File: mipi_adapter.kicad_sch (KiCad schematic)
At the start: 0 parts

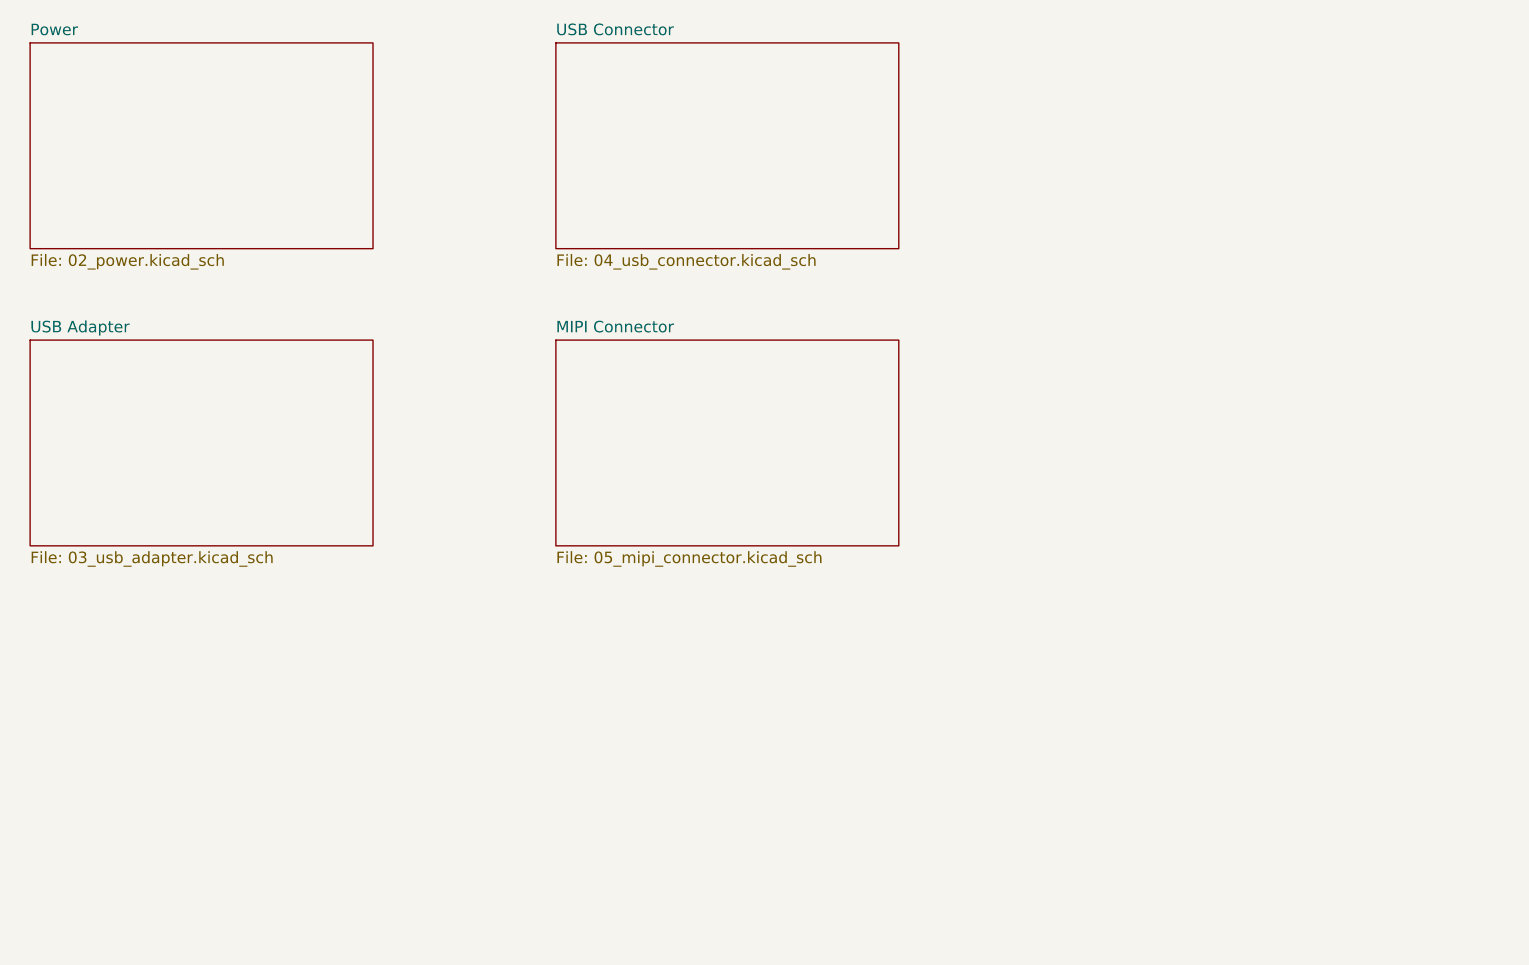
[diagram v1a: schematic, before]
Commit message: finished usb interface and added some new components
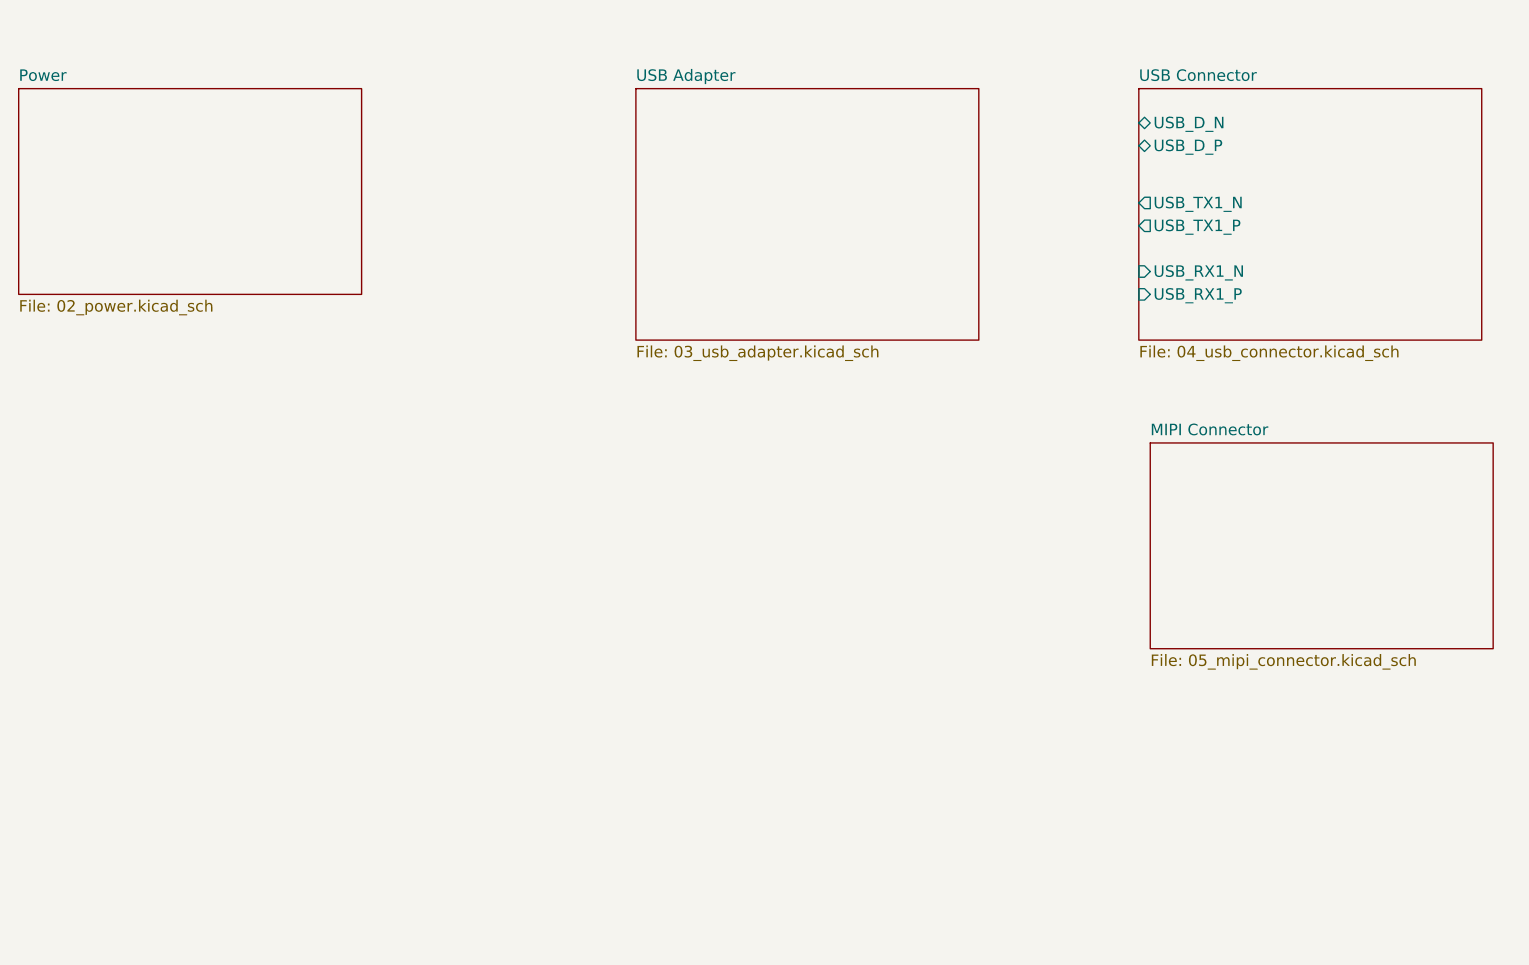
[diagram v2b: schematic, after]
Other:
- sheet USB Connector ports: added USB_D_N, USB_D_P, USB_RX1_N, USB_RX1_P, USB_TX1_N, USB_TX1_P; removed none

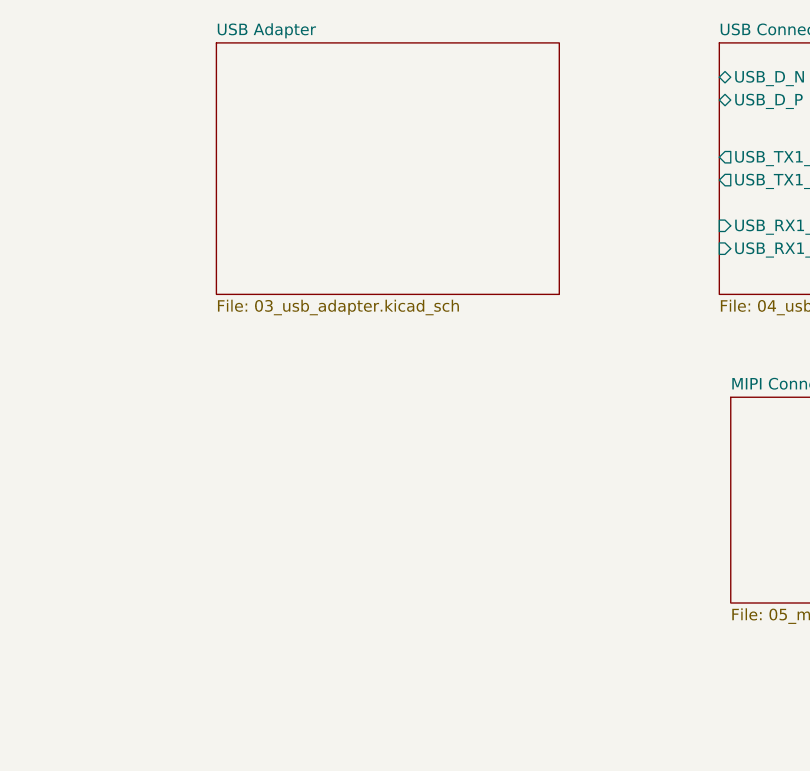
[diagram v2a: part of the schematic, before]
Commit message: added mipi connector
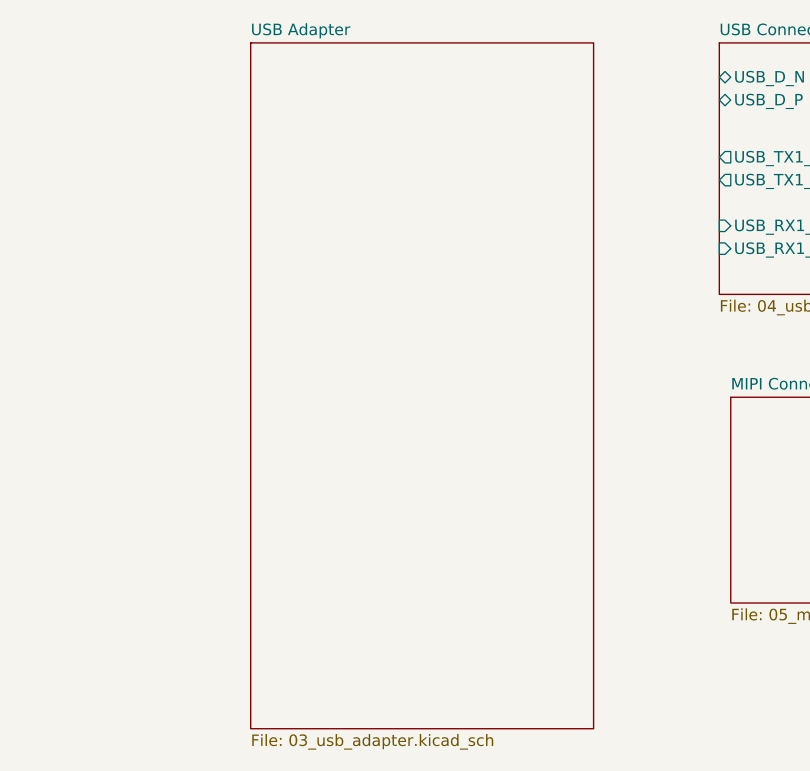
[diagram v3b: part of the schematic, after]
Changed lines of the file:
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@@
     )
   )
-  (sheet (at 120.65 38.1) (size 38.1 27.94) (fields_autoplaced)
+  (sheet (at 124.46 38.1) (size 38.1 76.2) (fields_autoplaced)
     (stroke (width 0.1524) (type solid) (color 0 0 0 0))
     (fill (color 0 0 0 0.0000))
-    (property "Sheet name" "USB Adapter" (id 0) (at 120.65 37.3884 0)
+    (property "Sheet name" "USB Adapter" (id 0) (at 124.46 37.3884 0)
       (effects (font (size 1.27 1.27)) (justify left bottom))
     )
-    (property "Sheet file" "03_usb_adapter.kicad_sch" (id 1) (at 120.65 66.6246 0)
+    (property "Sheet file" "03_usb_adapter.kicad_sch" (id 1) (at 124.46 114.8846 0)
       (effects (font (size 1.27 1.27)) (justify left top))
     )
@@
       (reference "#PWR?") (unit 1) (value "GND") (footprint "")
     )
+    (path "/5ba3e7e1-149c-4828-b319-acf737e6a433/3f044162-271a-4ddd-8981-66ada45c56ba"
+      (reference "#PWR?") (unit 1) (value "GND") (footprint "")
+    )
     (path "/91051729-874d-43f0-a1a2-c7d950b2f975/44a9e368-797f-4e49-af61-39d6bd303159"
       (reference "#PWR?") (unit 1) (value "GND") (footprint "")
@@
     )
     (path "/04c47af7-8e31-40d3-be90-665023313120/5c20341e-b213-4359-a245-c3606d6c5a60"
+      (reference "#PWR?") (unit 1) (value "GND") (footprint "")
+    )
+    (path "/5ba3e7e1-149c-4828-b319-acf737e6a433/5cce802a-9482-4067-8ddb-390b10df9ad4"
+      (reference "#PWR?") (unit 1) (value "+3.3V") (footprint "")
+    )
+    (path "/b35d25bb-a518-469d-9a23-fb54c00ba45e/5fab12b7-aec4-4625-aba8-d59b80f08db7"
       (reference "#PWR?") (unit 1) (value "GND") (footprint "")
     )
@@
       (reference "#PWR?") (unit 1) (value "+1V2") (footprint "")
     )
+    (path "/b35d25bb-a518-469d-9a23-fb54c00ba45e/a2a7ff45-64a1-4f59-b2a6-d02d88d80751"
+      (reference "#PWR?") (unit 1) (value "+3.3V") (footprint "")
+    )
     (path "/91051729-874d-43f0-a1a2-c7d950b2f975/a2e81052-9fa7-4bd5-8cf9-16777a877cf3"
       (reference "#PWR?") (unit 1) (value "GND") (footprint "")
@@
     (path "/91051729-874d-43f0-a1a2-c7d950b2f975/aa53df10-cec0-4613-a07b-eccf05edb333"
       (reference "#PWR?") (unit 1) (value "+1V2") (footprint "")
+    )
+    (path "/5ba3e7e1-149c-4828-b319-acf737e6a433/ab92135e-c45d-4a6c-a55b-5d5a82c9ce58"
+      (reference "#PWR?") (unit 1) (value "+3.3V") (footprint "")
     )
     (path "/91051729-874d-43f0-a1a2-c7d950b2f975/ae7dbec5-92ba-4d97-8ccf-e5b6147d8a86"
@@
       (reference "#PWR?") (unit 1) (value "+1V2") (footprint "")
     )
+    (path "/5ba3e7e1-149c-4828-b319-acf737e6a433/c519ef5c-193f-4d7d-a454-ff320a95ea05"
+      (reference "#PWR?") (unit 1) (value "GND") (footprint "")
+    )
     (path "/91051729-874d-43f0-a1a2-c7d950b2f975/c695fbd8-7519-405c-82e6-c90148ac5b4e"
       (reference "#PWR?") (unit 1) (value "GND") (footprint "")
@@
     (path "/91051729-874d-43f0-a1a2-c7d950b2f975/d64584dd-ff25-4305-83be-ba9ff21a6782"
       (reference "#PWR?") (unit 1) (value "+1V2") (footprint "")
+    )
+    (path "/b35d25bb-a518-469d-9a23-fb54c00ba45e/d85e11d7-bb26-4b16-bc38-f61c558f6752"
+      (reference "#PWR?") (unit 1) (value "GND") (footprint "")
     )
     (path "/91051729-874d-43f0-a1a2-c7d950b2f975/d988a57b-b5ef-4faf-b7a0-5e73f9a2b38e"
@@
       (reference "#PWR?") (unit 1) (value "GND") (footprint "")
     )
+    (path "/b35d25bb-a518-469d-9a23-fb54c00ba45e/0995a256-cbb5-4eed-a267-1fa499146e87"
+      (reference "C?") (unit 1) (value "0.1u") (footprint "Capacitor_SMD:C_0603_1608Metric")
+    )
     (path "/91051729-874d-43f0-a1a2-c7d950b2f975/108e7962-4cee-4064-9988-b3d032f6761b"
       (reference "C?") (unit 1) (value "2.2u") (footprint "CSI2USB:C_0805_2012Metric")
@@
       (reference "C?") (unit 1) (value "10n") (footprint "CSI2USB:C_0402_1005Metric")
     )
+    (path "/5ba3e7e1-149c-4828-b319-acf737e6a433/01001c7d-76fe-448c-ad61-6eaf16350c7e"
+      (reference "J?") (unit 1) (value "Conn_01x04_Male") (footprint "Connector_PinHeader_2.00mm:PinHeader_1x04_P2.00mm_Vertical")
+    )
+    (path "/5ba3e7e1-149c-4828-b319-acf737e6a433/12919009-6e4d-4402-a8b2-e60fbb5fd0e5"
+      (reference "J?") (unit 1) (value "Conn_01x02_Male") (footprint "")
+    )
     (path "/5ba3e7e1-149c-4828-b319-acf737e6a433/7d731779-3929-4adb-bfda-94d4a92794c1"
-      (reference "J?") (unit 1) (value "Conn_02x05_Odd_Even") (footprint "")
+      (reference "J?") (unit 1) (value "Conn_02x05_Odd_Even") (footprint "Connector_PinHeader_2.00mm:PinHeader_2x05_P2.00mm_Vertical")
+    )
+    (path "/b35d25bb-a518-469d-9a23-fb54c00ba45e/92dd3eb8-01c4-4850-8848-4d34abe3102b"
+      (reference "J?") (unit 1) (value "Conn_01x22") (footprint "Connector_FFC-FPC:Hirose_FH12-22S-0.5SH_1x22-1MP_P0.50mm_Horizontal")
     )
     (path "/91051729-874d-43f0-a1a2-c7d950b2f975/16b93a7c-6fdd-4c0c-9db9-71f48ba88d06"
@@
       (reference "R?") (unit 1) (value "10k") (footprint "Resistor_SMD:R_0603_1608Metric")
     )
+    (path "/5ba3e7e1-149c-4828-b319-acf737e6a433/1ab54462-42d4-42d7-a80e-9568b0a1e6f9"
+      (reference "R?") (unit 1) (value "10k") (footprint "Resistor_SMD:R_0603_1608Metric")
+    )
     (path "/91051729-874d-43f0-a1a2-c7d950b2f975/1e91a111-7148-4509-9412-b072b97a5aa3"
       (reference "R?") (unit 1) (value "100k") (footprint "Resistor_SMD:R_0603_1608Metric")
     )
+    (path "/b35d25bb-a518-469d-9a23-fb54c00ba45e/23e4942d-c12a-4f4f-9dd0-282c3bb22f6c"
+      (reference "R?") (unit 1) (value "0") (footprint "Resistor_SMD:R_0603_1608Metric")
+    )
     (path "/91051729-874d-43f0-a1a2-c7d950b2f975/253ca4b1-4798-4b8a-9ba5-0b1d3f3078ad"
       (reference "R?") (unit 1) (value "0") (footprint "Resistor_SMD:R_0603_1608Metric")
@@
       (reference "R?") (unit 1) (value "0") (footprint "Resistor_SMD:R_0603_1608Metric")
     )
+    (path "/5ba3e7e1-149c-4828-b319-acf737e6a433/7069c73c-a03f-412b-b527-29fedb0fa722"
+      (reference "R?") (unit 1) (value "100") (footprint "Resistor_SMD:R_0603_1608Metric")
+    )
     (path "/91051729-874d-43f0-a1a2-c7d950b2f975/7ce0f863-f3ae-4ef9-86e4-8830a7bce510"
       (reference "R?") (unit 1) (value "150k") (footprint "Resistor_SMD:R_0603_1608Metric")
@@
       (reference "R?") (unit 1) (value "0") (footprint "Resistor_SMD:R_0603_1608Metric")
     )
+    (path "/5ba3e7e1-149c-4828-b319-acf737e6a433/9dbc2ec6-035c-4a7a-b2b0-e9c3b10478c8"
+      (reference "R?") (unit 1) (value "10k") (footprint "Resistor_SMD:R_0603_1608Metric")
+    )
     (path "/91051729-874d-43f0-a1a2-c7d950b2f975/a3ac6d31-82c4-4edb-a1ab-e9f9daa2547b"
       (reference "R?") (unit 1) (value "100k") (footprint "Resistor_SMD:R_0603_1608Metric")
@@
       (reference "R?") (unit 1) (value "100") (footprint "Resistor_SMD:R_0603_1608Metric")
     )
+    (path "/5ba3e7e1-149c-4828-b319-acf737e6a433/b31ce4d2-6031-4fae-ae91-d7cb73af731e"
+      (reference "R?") (unit 1) (value "10k") (footprint "Resistor_SMD:R_0603_1608Metric")
+    )
     (path "/5ba3e7e1-149c-4828-b319-acf737e6a433/beffeab7-96c4-4894-bae2-9be6374b5a52"
       (reference "R?") (unit 1) (value "100") (footprint "Resistor_SMD:R_0603_1608Metric")
@@
       (reference "U?") (unit 1) (value "AP3402") (footprint "Package_TO_SOT_SMD:TSOT-23-6")
     )
+    (path "/5ba3e7e1-149c-4828-b319-acf737e6a433/f1a6e7f8-e27d-4a54-ae2a-f079d14a16fa"
+      (reference "U?") (unit 1) (value "74LVC2G17") (footprint "")
+    )
     (path "/91051729-874d-43f0-a1a2-c7d950b2f975/22773e1e-1059-4f1d-9db6-d12bbfaabfab"
       (reference "U?") (unit 2) (value "CYUSB306X") (footprint "Package_BGA:XBGA-121_10x10mm_Layout11x11_P0.8mm")
@@
       (reference "U?") (unit 2) (value "PCMF2USB3S") (footprint "samaritan:Nexperia_WLCSP-10_4-2-4_1.57x1.17mm_Layout6x3_P0.4mm")
     )
+    (path "/5ba3e7e1-149c-4828-b319-acf737e6a433/7ad44938-68fe-4ebd-9571-95e08fd7986e"
+      (reference "U?") (unit 2) (value "74LVC2G17") (footprint "")
+    )
     (path "/5ba3e7e1-149c-4828-b319-acf737e6a433/be44dec8-9217-4f23-95b9-0a739ea0060c"

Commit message: finished first pass of the schematics
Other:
- sheet USB Adapter renamed CPU
- sheet CPU ports: added MIPI_CLK_N, MIPI_CLK_P, MIPI_D0_N, MIPI_D0_P, MIPI_D1_N, MIPI_D1_P, MIPI_D2_N, MIPI_D2_P, MIPI_D3_N, MIPI_D3_P, MIPI_I2C_SCL, MIPI_I2C_SDA, MIPI_MCLK, USB_D_N, USB_D_P, USB_RX1_N, USB_RX1_P, USB_TX1_N, USB_TX1_P; removed none
- sheet MIPI Connector ports: added MIPI_CLK_N, MIPI_CLK_P, MIPI_D0_N, MIPI_D0_P, MIPI_D1_N, MIPI_D1_P, MIPI_D2_N, MIPI_D2_P, MIPI_D3_N, MIPI_D3_P, MIPI_I2C_SCL, MIPI_I2C_SDA; removed none
